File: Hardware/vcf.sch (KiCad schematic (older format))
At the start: 0 parts

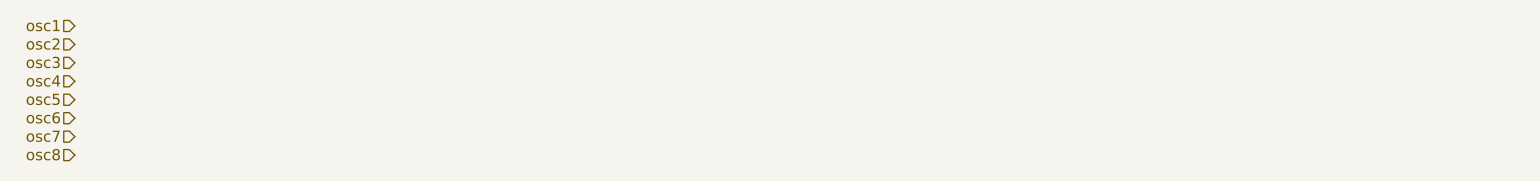
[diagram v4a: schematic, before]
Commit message: complete wiring of top level schematic hierarchical pages
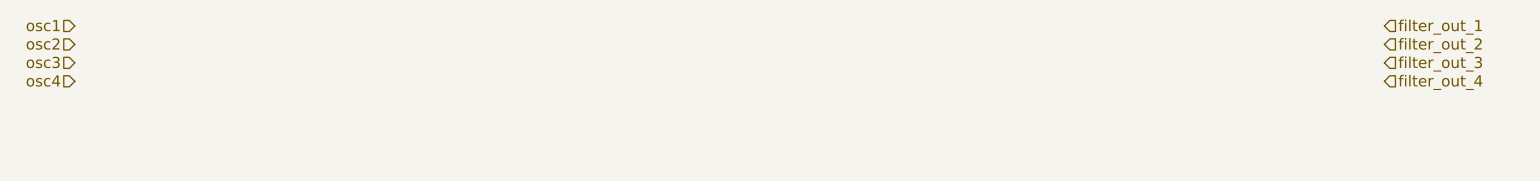
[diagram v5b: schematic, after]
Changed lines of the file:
@@
 Text HLabel 1700 1650 0    60   Input ~ 0
 osc4
-Text HLabel 1700 1750 0    60   Input ~ 0
-osc5
-Text HLabel 1700 1850 0    60   Input ~ 0
-osc6
-Text HLabel 1700 1950 0    60   Input ~ 0
-osc7
-Text HLabel 1700 2050 0    60   Input ~ 0
-osc8
+Text HLabel 8800 1350 2    60   Input ~ 0
+filter_out_1
+Text HLabel 8800 1450 2    60   Input ~ 0
+filter_out_2
+Text HLabel 8800 1550 2    60   Input ~ 0
+filter_out_3
+Text HLabel 8800 1650 2    60   Input ~ 0
+filter_out_4
 $EndSCHEMATC

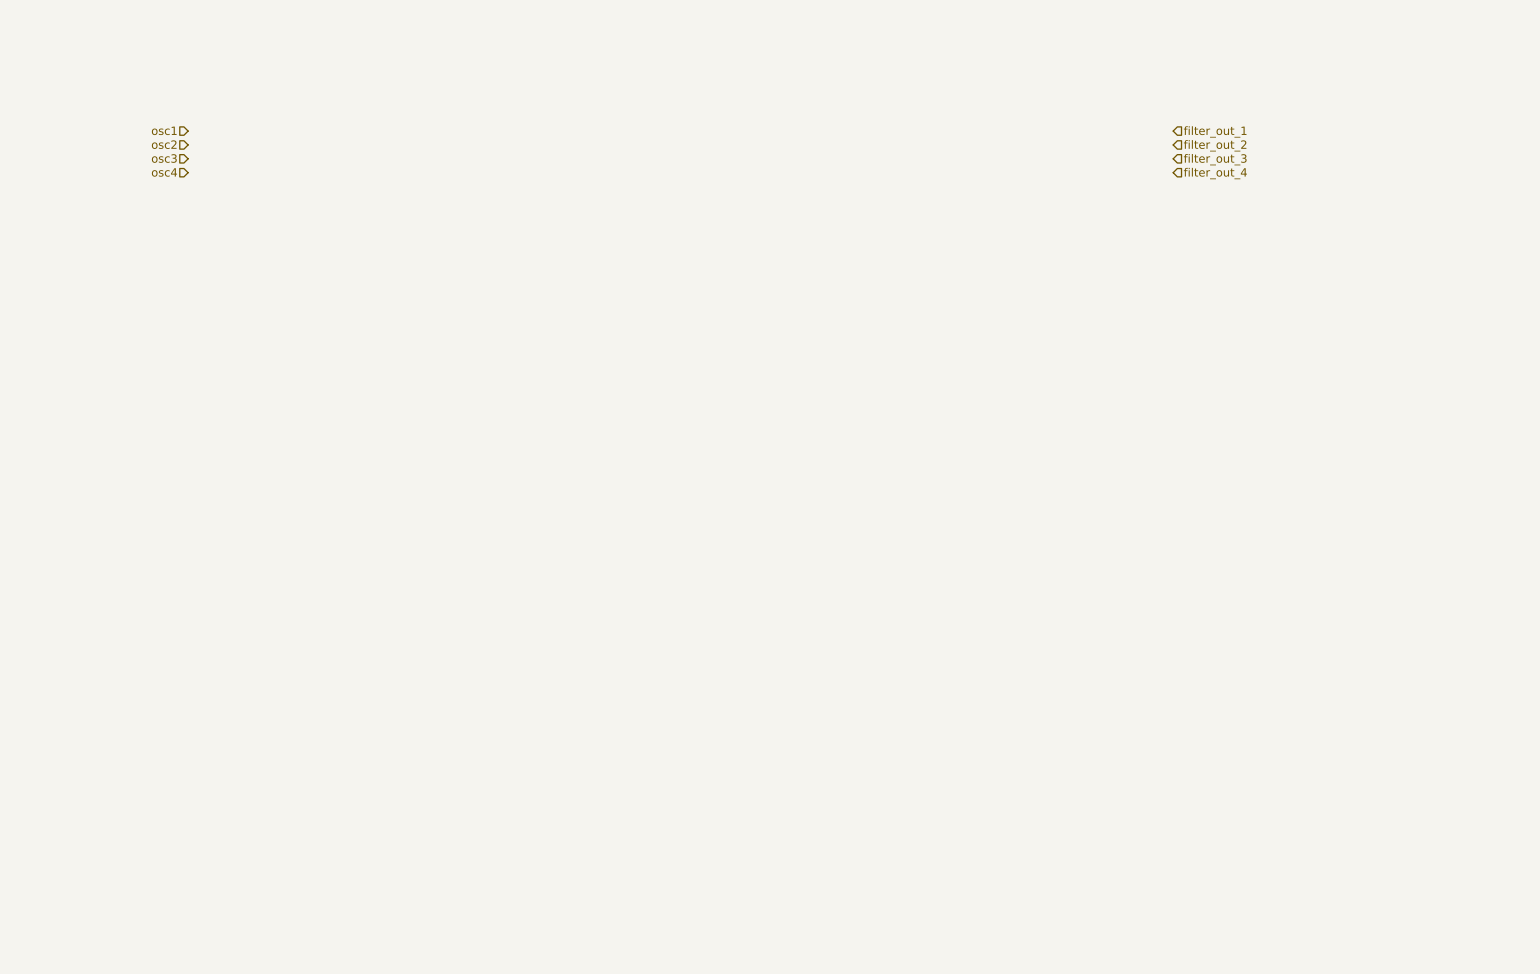
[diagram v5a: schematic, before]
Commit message: complete filters for all 4 oscs
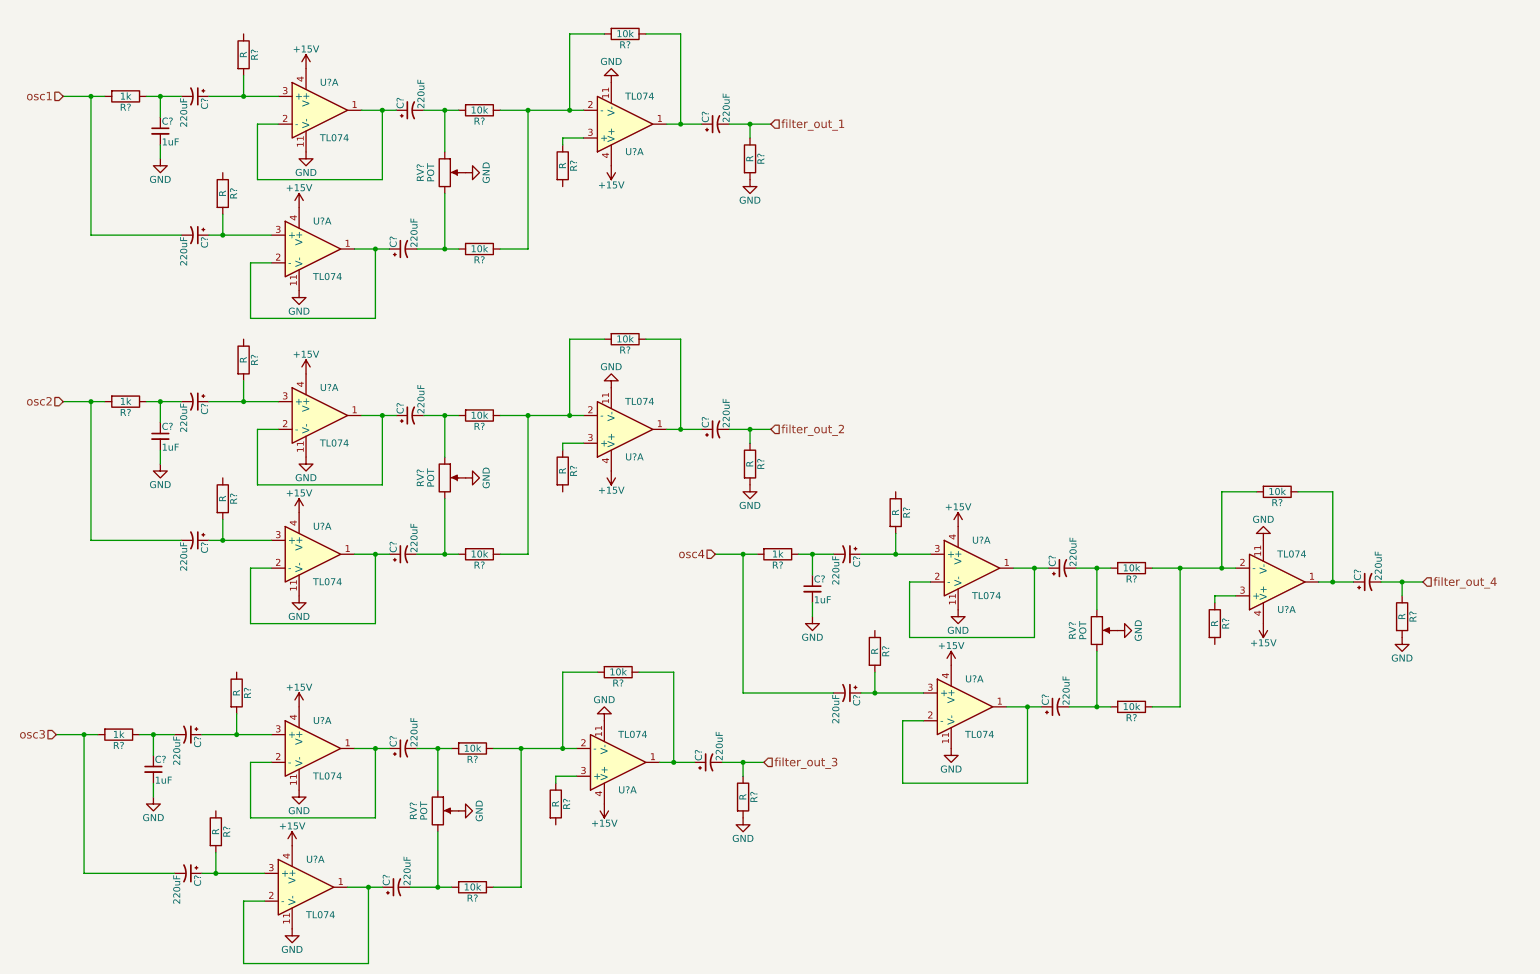
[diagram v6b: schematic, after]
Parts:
- added C? (x4): 1uF, symbol C_Small
- added C? (x20): 220uF, symbol CP1_Small
- added R? (x4): 1k, symbol R
- added R? (x16): R, symbol R
- added R? (x12): 10k, symbol R
- added RV? (x4): POT, symbol POT
- added U? (x12): TL074, symbol TL074
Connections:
- net filter_out_1: now also C?.2, R?.1
- net filter_out_2: now also C?.2, R?.1
- net filter_out_3: now also C?.2, R?.1
- net filter_out_4: now also C?.2, R?.1
- net osc1: now also C?.2, R?.2
- net osc2: now also C?.2, R?.2
- net osc3: now also C?.2, R?.2
- net osc4: now also C?.2, R?.2
- new net: C?.1, C?.2, R?.1 (x4)
- new net: C?.1, U?.1, U?.2 (-) (x8)
- new net: C?.1, R?.2, U?.3 (+) (x8)
- new net: C?.2, R?.2, RV?.1 (x4)
- new net: C?.2, R?.2, RV?.3 (x4)
- new net: R?.1, R?.1, R?.2, U?.2 (-) (x4)
- new net: C?.1, R?.1, U?.1 (x4)
- new net: R?.1, U?.3 (+) (x4)
- new net +15V: U?.4 (V+), U?.4 (V+), U?.4 (V+), U?.4 (V+), U?.4 (V+), U?.4 (V+), U?.4 (V+), U?.4 (V+), U?.4 (V+), U?.4 (V+), U?.4 (V+), U?.4 (V+)
- new net GND: C?.2, C?.2, C?.2, C?.2, R?.2, R?.2, R?.2, R?.2, RV?.2, RV?.2, RV?.2, RV?.2, U?.11 (V-), U?.11 (V-), U?.11 (V-), U?.11 (V-), U?.11 (V-), U?.11 (V-), U?.11 (V-), U?.11 (V-), U?.11 (V-), U?.11 (V-), U?.11 (V-), U?.11 (V-)

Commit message: add power jack, 3.3V regulator, VREF divider
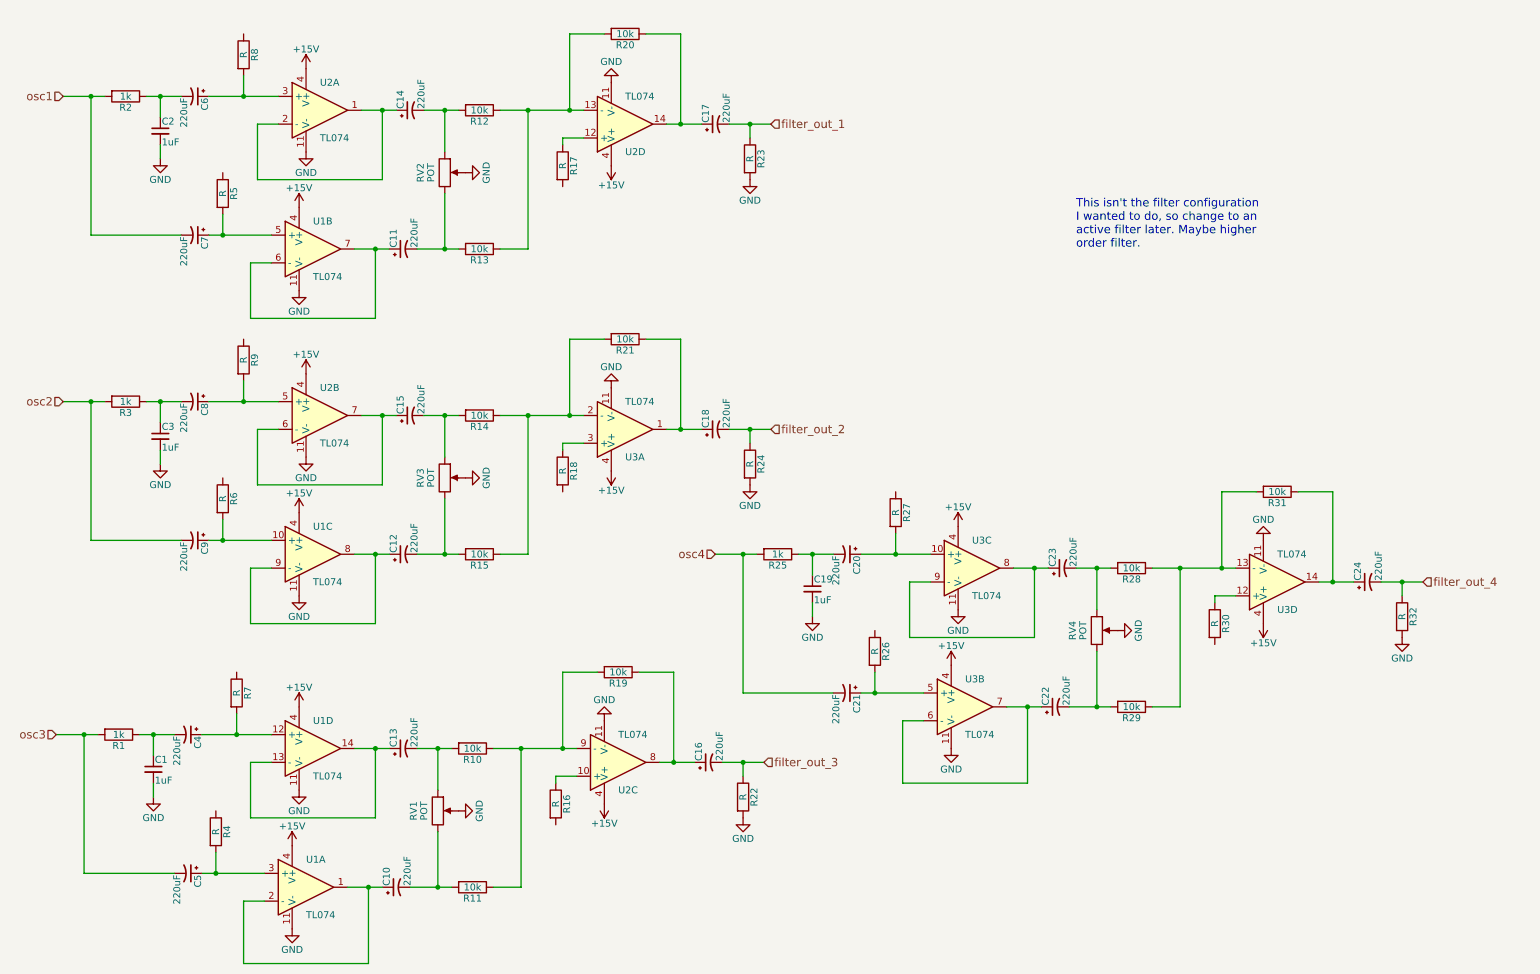
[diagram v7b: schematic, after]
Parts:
- gave numbers to parts that had none: 63
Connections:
- net at C7.1, R5.2: now also U1.5 (+); no longer U1.3 (+)
- net at R12.1, R13.1, R20.2: now also U2.13 (-); no longer U2.2 (-)
- net at C17.1, R20.1: now also U2.14; no longer U2.1
- net at R17.1: now also U2.12 (+); no longer U2.3 (+)
- net at C8.1, R9.2: now also U2.5 (+); no longer U2.3 (+)
- net at C9.1, R6.2: now also U1.10 (+); no longer U1.3 (+)
- net at C4.1, R7.2: now also U1.12 (+); no longer U1.3 (+)
- net at R10.1, R11.1, R19.2: now also U2.9 (-); no longer U2.2 (-)
- net at C16.1, R19.1: now also U2.8; no longer U2.1
- net at R16.1: now also U2.10 (+); no longer U2.3 (+)
- net at C20.1, R27.2: now also U3.10 (+); no longer U3.3 (+)
- net at C21.1, R26.2: now also U3.5 (+); no longer U3.3 (+)
- net at R28.1, R29.1, R31.2: now also U3.13 (-); no longer U3.2 (-)
- net at C24.1, R31.1: now also U3.14; no longer U3.1
- net at R30.1: now also U3.12 (+); no longer U3.3 (+)
- new net: C11.1, U1.6 (-), U1.7
- new net: C15.1, U2.6 (-), U2.7
- new net: C12.1, U1.8, U1.9 (-)
- new net: C13.1, U1.13 (-), U1.14
- new net: C23.1, U3.8, U3.9 (-)
- new net: C22.1, U3.6 (-), U3.7
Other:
- note added: "This isn't the filter configuration \nI wanted to do, so change to an \nactive filter later. Maybe higher \norder filter."

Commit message: add VREF to all single supply op amps
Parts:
- R16, R17, R18, R26, R27, R30, R4, R5, R6, R7, R8, R9: value R -> 470k
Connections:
- net VREF: now reaches R8.1
- net VREF: now also R16.2, R17.2, R18.2, R26.1, R27.1, R30.2, R4.1, R5.1, R6.1, R7.1, R9.1
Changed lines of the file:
@@
 $Descr A4 11693 8268
 encoding utf-8
-Sheet 2 8
+Sheet 2 7
 Title ""
 Date ""
@@
 P 2100 800
 F 0 "R8" V 2180 800 50  0000 C CNN
-F 1 "R" V 2100 800 50  0000 C CNN
+F 1 "470k" V 2100 800 50  0000 C CNN
 F 2 "" V 2030 800 50  0001 C CNN
 F 3 "" H 2100 800 50  0001 C CNN
@@
 P 1950 1800
 F 0 "R5" V 2030 1800 50  0000 C CNN
-F 1 "R" V 1950 1800 50  0000 C CNN
+F 1 "470k" V 1950 1800 50  0000 C CNN
 F 2 "" V 1880 1800 50  0001 C CNN
 F 3 "" H 1950 1800 50  0001 C CNN
@@
 P 4400 1600
 F 0 "R17" V 4480 1600 50  0000 C CNN
-F 1 "R" V 4400 1600 50  0000 C CNN
+F 1 "470k" V 4400 1600 50  0000 C CNN
 F 2 "" V 4330 1600 50  0001 C CNN
 F 3 "" H 4400 1600 50  0001 C CNN
@@
 P 2100 3000
 F 0 "R9" V 2180 3000 50  0000 C CNN
-F 1 "R" V 2100 3000 50  0000 C CNN
+F 1 "470k" V 2100 3000 50  0000 C CNN
 F 2 "" V 2030 3000 50  0001 C CNN
 F 3 "" H 2100 3000 50  0001 C CNN
@@
 P 1950 4000
 F 0 "R6" V 2030 4000 50  0000 C CNN
-F 1 "R" V 1950 4000 50  0000 C CNN
+F 1 "470k" V 1950 4000 50  0000 C CNN
 F 2 "" V 1880 4000 50  0001 C CNN
 F 3 "" H 1950 4000 50  0001 C CNN
@@
 P 4400 3800
 F 0 "R18" V 4480 3800 50  0000 C CNN
-F 1 "R" V 4400 3800 50  0000 C CNN
+F 1 "470k" V 4400 3800 50  0000 C CNN
 F 2 "" V 4330 3800 50  0001 C CNN
 F 3 "" H 4400 3800 50  0001 C CNN
@@
 P 2050 5400
 F 0 "R7" V 2130 5400 50  0000 C CNN
-F 1 "R" V 2050 5400 50  0000 C CNN
+F 1 "470k" V 2050 5400 50  0000 C CNN
 F 2 "" V 1980 5400 50  0001 C CNN
 F 3 "" H 2050 5400 50  0001 C CNN
@@
 P 1900 6400
 F 0 "R4" V 1980 6400 50  0000 C CNN
-F 1 "R" V 1900 6400 50  0000 C CNN
+F 1 "470k" V 1900 6400 50  0000 C CNN
 F 2 "" V 1830 6400 50  0001 C CNN
 F 3 "" H 1900 6400 50  0001 C CNN
@@
 P 4350 6200
 F 0 "R16" V 4430 6200 50  0000 C CNN
-F 1 "R" V 4350 6200 50  0000 C CNN
+F 1 "470k" V 4350 6200 50  0000 C CNN
 F 2 "" V 4280 6200 50  0001 C CNN
 F 3 "" H 4350 6200 50  0001 C CNN
@@
 P 6800 4100
 F 0 "R27" V 6880 4100 50  0000 C CNN
-F 1 "R" V 6800 4100 50  0000 C CNN
+F 1 "470k" V 6800 4100 50  0000 C CNN
 F 2 "" V 6730 4100 50  0001 C CNN
 F 3 "" H 6800 4100 50  0001 C CNN
@@
 P 6650 5100
 F 0 "R26" V 6730 5100 50  0000 C CNN
-F 1 "R" V 6650 5100 50  0000 C CNN
+F 1 "470k" V 6650 5100 50  0000 C CNN
 F 2 "" V 6580 5100 50  0001 C CNN
 F 3 "" H 6650 5100 50  0001 C CNN
@@
 P 9100 4900
 F 0 "R30" V 9180 4900 50  0000 C CNN
-F 1 "R" V 9100 4900 50  0000 C CNN
+F 1 "470k" V 9100 4900 50  0000 C CNN
 F 2 "" V 9030 4900 50  0001 C CNN
 F 3 "" H 9100 4900 50  0001 C CNN
@@
 Text Notes 8100 2200 0    60   ~ 0
 This isn't the filter configuration \nI wanted to do, so change to an \nactive filter later. Maybe higher \norder filter.
+Text GLabel 2000 550  0    60   Input ~ 0
+VREF
+Wire Wire Line
+	2000 550  2100 550
+Wire Wire Line
+	2100 550  2100 650
+Text GLabel 1900 1550 0    60   Input ~ 0
+VREF
+Wire Wire Line
+	1900 1550 1950 1550
+Wire Wire Line
+	1950 1550 1950 1650
+Text GLabel 2000 2800 0    60   Input ~ 0
+VREF
+Wire Wire Line
+	2000 2800 2100 2800
+Wire Wire Line
+	2100 2800 2100 2850
+Text GLabel 1900 3800 0    60   Input ~ 0
+VREF
+Wire Wire Line
+	1900 3800 1950 3800
+Wire Wire Line
+	1950 3800 1950 3850
+Text GLabel 2000 5200 0    60   Input ~ 0
+VREF
+Wire Wire Line
+	2000 5200 2050 5200
+Wire Wire Line
+	2050 5200 2050 5250
+Text GLabel 1850 6200 0    60   Input ~ 0
+VREF
+Wire Wire Line
+	1850 6200 1900 6200
+Wire Wire Line
+	1900 6200 1900 6250
+Text GLabel 4400 1850 3    60   Input ~ 0
+VREF
+Wire Wire Line
+	4400 1850 4400 1750
+Text GLabel 4400 4050 3    60   Input ~ 0
+VREF
+Wire Wire Line
+	4400 4050 4400 3950
+Text GLabel 4350 6400 3    60   Input ~ 0
+VREF
+Wire Wire Line
+	4350 6400 4350 6350
+Text GLabel 6750 3900 0    60   Input ~ 0
+VREF
+Wire Wire Line
+	6750 3900 6800 3900
+Wire Wire Line
+	6800 3900 6800 3950
+Text GLabel 6600 4900 0    60   Input ~ 0
+VREF
+Wire Wire Line
+	6600 4900 6650 4900
+Wire Wire Line
+	6650 4900 6650 4950
+Text GLabel 9100 5100 3    60   Input ~ 0
+VREF
+Wire Wire Line
+	9100 5100 9100 5050
 $EndSCHEMATC
